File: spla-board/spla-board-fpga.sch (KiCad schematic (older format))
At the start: 35 parts, among them J2 J_JTAG, U1 LFE5U-45F-BG256

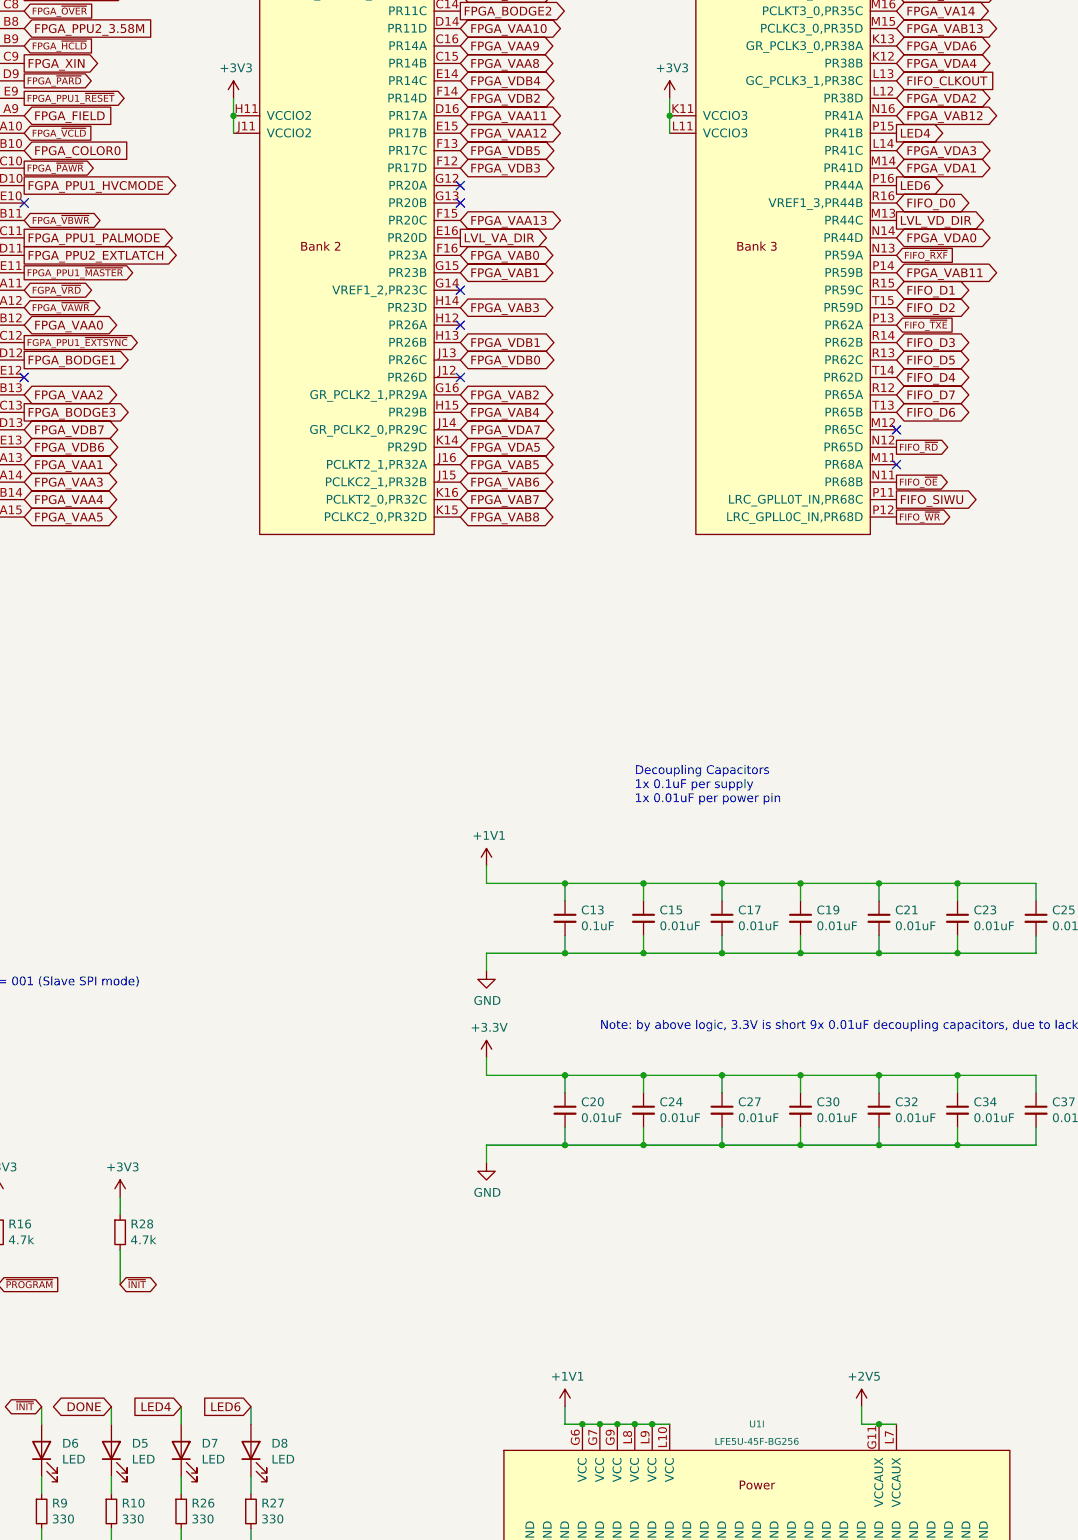
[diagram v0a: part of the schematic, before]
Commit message: schematic: Rename LED[46] to LED[78], to match silkscreen.
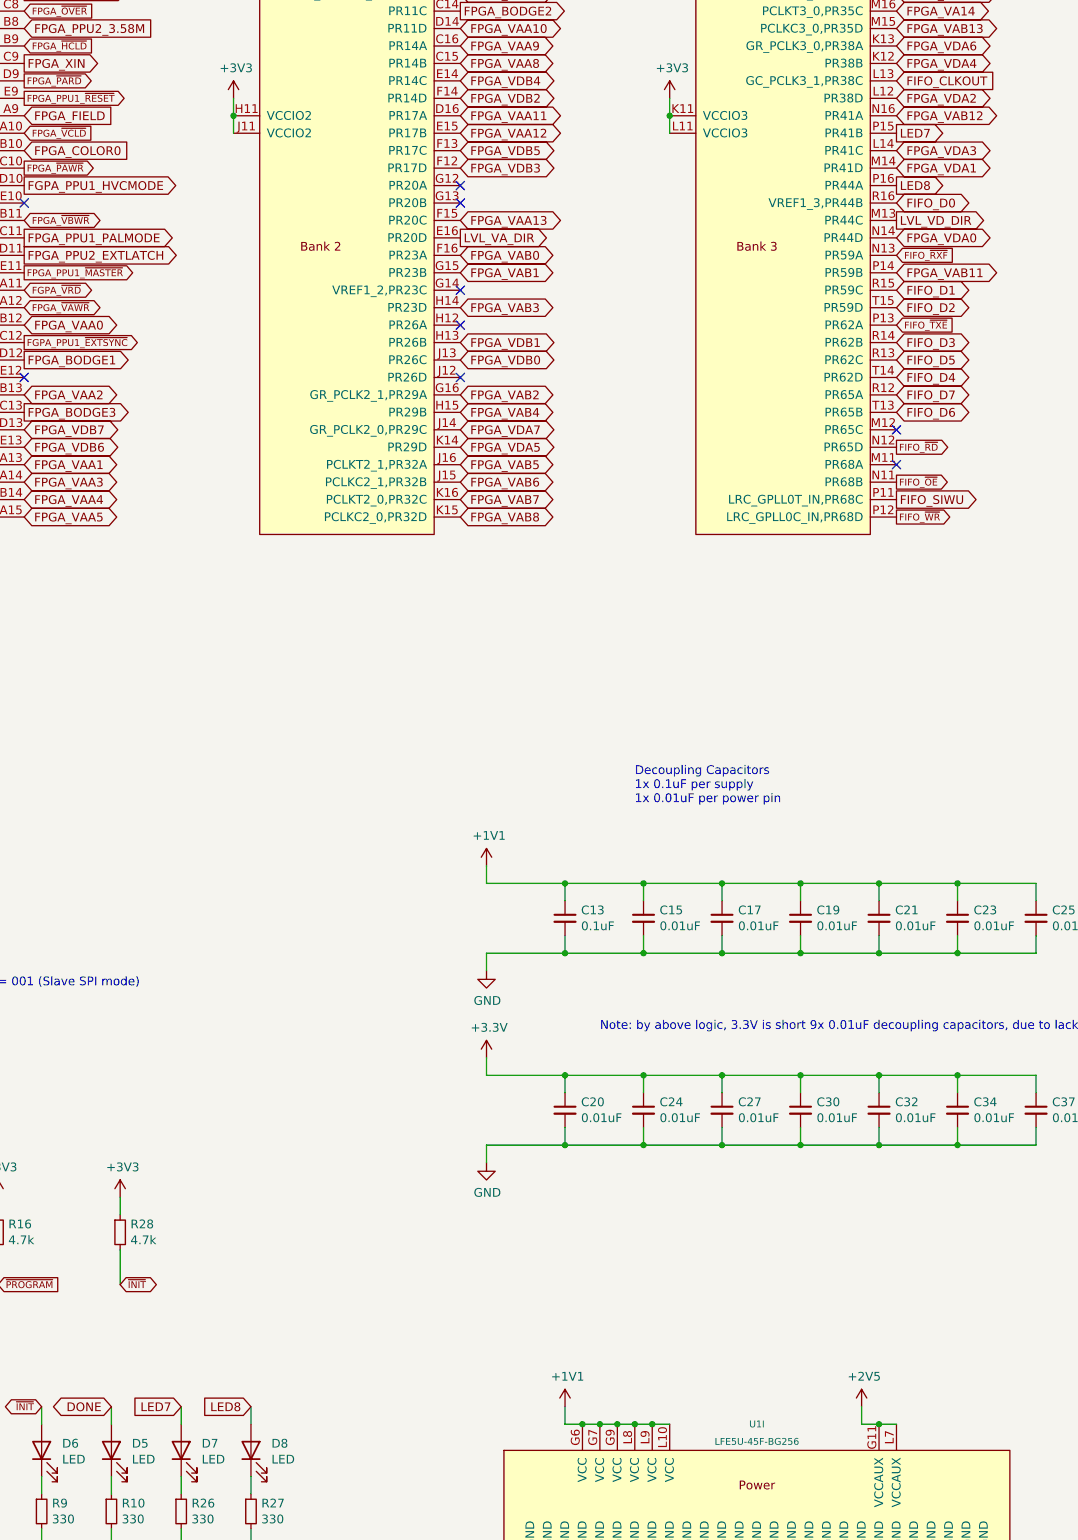
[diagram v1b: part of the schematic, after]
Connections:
- net LED4 renamed LED7
- net LED6 renamed LED8
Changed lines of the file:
@@
 	5950 9500 5950 9600
 Text GLabel 5550 9500 0    50   Input ~ 0
-LED4
+LED7
 Text GLabel 5950 9500 0    50   Input ~ 0
-LED6
+LED8
 Text GLabel 9650 2200 2    50   Output ~ 0
-LED4
+LED7
 Text GLabel 9650 2500 2    50   Output ~ 0
-LED6
+LED8
 NoConn ~ 9650 4100
 NoConn ~ 9650 3900

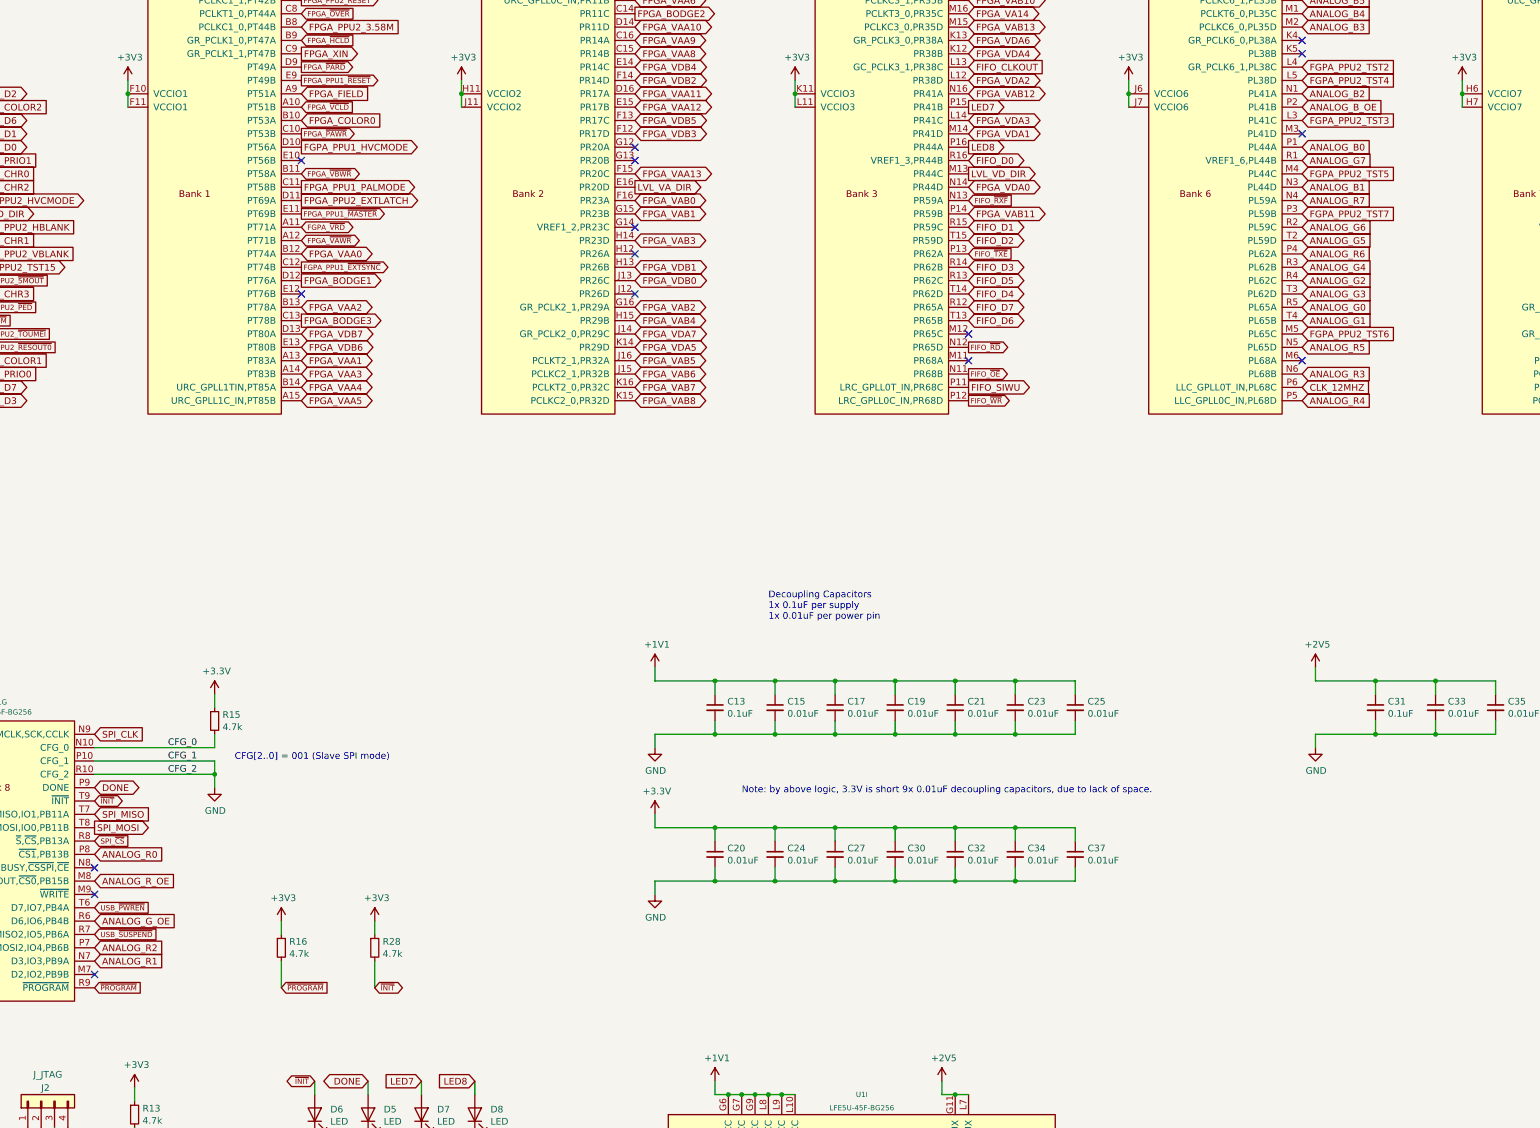
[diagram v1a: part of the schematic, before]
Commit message: schematic/pcb: Consolidate analog output-enable nets, and add a pullup resistor.
Note that this leaves two FPGA pins unused, which I'll need to correct later.
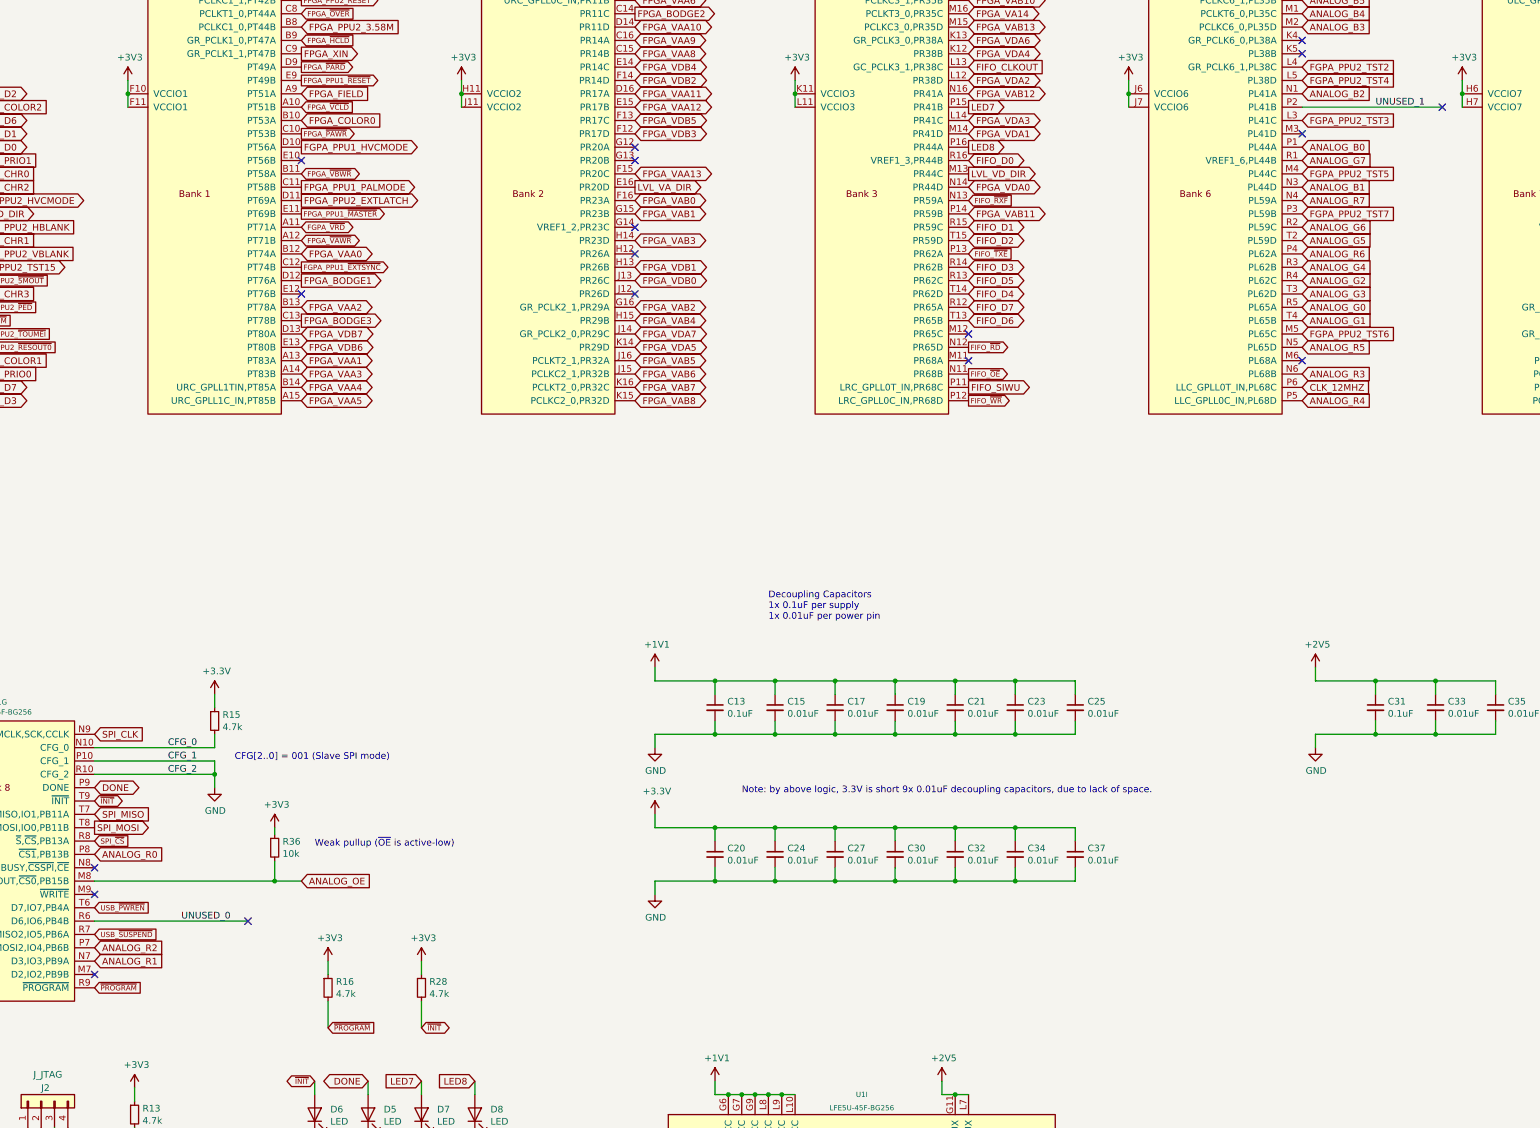
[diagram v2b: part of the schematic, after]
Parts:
- added R36: 10k, Resistor_SMD:R_0603_1608Metric, symbol Device:R_Small
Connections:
- net +3V3: now also R36.1
- net ANALOG_B_OE renamed UNUSED_1
- net ANALOG_G_OE renamed UNUSED_0
- net ANALOG_R_OE renamed ANALOG_OE
- net ANALOG_OE: now also R36.2
- no-connect marks 18 -> 20
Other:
- note added: "Weak pullup (~OE~ is active-low)"
- moved on the sheet: R16, R28
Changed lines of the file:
@@
 Text GLabel 12150 4300 2    50   Input ~ 0
 CLK_12MHZ
-Text GLabel 12150 2200 2    50   Input ~ 0
-ANALOG_B_OE
 Wire Wire Line
 	13350 2100 13350 2200
@@
 Text GLabel 14650 4400 2    50   Input ~ 0
 ANALOG_B7
-Text GLabel 3100 8300 2    50   Input ~ 0
-ANALOG_G_OE
-Text GLabel 3100 8000 2    50   Input ~ 0
-ANALOG_R_OE
+Text GLabel 4650 8000 2    50   Input ~ 0
+ANALOG_OE
 Text GLabel 12150 3700 2    50   Input ~ 0
 ANALOG_G0
@@
 Wire Wire Line
 	4000 6600 4000 6700
-Text GLabel 4500 8800 2    39   Input ~ 0
+Text GLabel 4850 9100 2    39   Input ~ 0
 ~PROGRAM
 Wire Wire Line
-	4500 8800 4500 8600
+	4850 9100 4850 8900
 $Comp
 L Device:R_Small R?
 U 1 1 5EB9F9F9
-P 4500 8500
+P 4850 8800
 AR Path="/5E4F712F/5EB9F9F9" Ref="R?"  Part="1"
 AR Path="/5E50D39B/5EB9F9F9" Ref="R?"  Part="1"
 AR Path="/5E4D8358/5EB9F9F9" Ref="R16"  Part="1"
-F 0 "R16" H 4559 8546 50  0000 L CNN
-F 1 "4.7k" H 4559 8455 50  0000 L CNN
-F 2 "Resistor_SMD:R_0603_1608Metric" H 4500 8500 50  0001 C CNN
-F 3 "~" H 4500 8500 50  0001 C CNN
-F 4 "RMCF0603JT4K70CT-ND" H 4500 8500 50  0001 C CNN "Digikey"
-F 5 "Stackpole Electronics Inc" H 4500 8500 50  0001 C CNN "Manufacturer"
-F 6 "RMCF0603JT4K70" H 4500 8500 50  0001 C CNN "Manufacturer Id"
-	1    4500 8500
+F 0 "R16" H 4909 8846 50  0000 L CNN
+F 1 "4.7k" H 4909 8755 50  0000 L CNN
+F 2 "Resistor_SMD:R_0603_1608Metric" H 4850 8800 50  0001 C CNN
+F 3 "~" H 4850 8800 50  0001 C CNN
+F 4 "RMCF0603JT4K70CT-ND" H 4850 8800 50  0001 C CNN "Digikey"
+F 5 "Stackpole Electronics Inc" H 4850 8800 50  0001 C CNN "Manufacturer"
+F 6 "RMCF0603JT4K70" H 4850 8800 50  0001 C CNN "Manufacturer Id"
+	1    4850 8800
 	1    0    0    -1
 $EndComp
@@
 L power:+3V3 #PWR0214
 U 1 1 5EBA4221
-P 4500 8300
-F 0 "#PWR0214" H 4500 8150 50  0001 C CNN
-F 1 "+3V3" H 4515 8473 50  0000 C CNN
-F 2 "" H 4500 8300 50  0001 C CNN
-F 3 "" H 4500 8300 50  0001 C CNN
-	1    4500 8300
-	1    0    0    -1
-$EndComp
-Wire Wire Line
-	4500 8300 4500 8400
-Text GLabel 5200 8800 2    39   BiDi ~ 0
+P 4850 8600
+F 0 "#PWR0214" H 4850 8450 50  0001 C CNN
+F 1 "+3V3" H 4865 8773 50  0000 C CNN
+F 2 "" H 4850 8600 50  0001 C CNN
+F 3 "" H 4850 8600 50  0001 C CNN
+	1    4850 8600
+	1    0    0    -1
+$EndComp
+Wire Wire Line
+	4850 8600 4850 8700
+Text GLabel 5550 9100 2    39   BiDi ~ 0
 ~INIT
 Wire Wire Line
-	5200 8800 5200 8600
+	5550 9100 5550 8900
 $Comp
 L Device:R_Small R?
 U 1 1 5EBAC32F
-P 5200 8500
+P 5550 8800
 AR Path="/5E4F712F/5EBAC32F" Ref="R?"  Part="1"
 AR Path="/5E50D39B/5EBAC32F" Ref="R?"  Part="1"
 AR Path="/5E4D8358/5EBAC32F" Ref="R28"  Part="1"
-F 0 "R28" H 5259 8546 50  0000 L CNN
-F 1 "4.7k" H 5259 8455 50  0000 L CNN
-F 2 "Resistor_SMD:R_0603_1608Metric" H 5200 8500 50  0001 C CNN
-F 3 "~" H 5200 8500 50  0001 C CNN
-F 4 "RMCF0603JT4K70CT-ND" H 5200 8500 50  0001 C CNN "Digikey"
-F 5 "Stackpole Electronics Inc" H 5200 8500 50  0001 C CNN "Manufacturer"
-F 6 "RMCF0603JT4K70" H 5200 8500 50  0001 C CNN "Manufacturer Id"
-	1    5200 8500
+F 0 "R28" H 5609 8846 50  0000 L CNN
+F 1 "4.7k" H 5609 8755 50  0000 L CNN
+F 2 "Resistor_SMD:R_0603_1608Metric" H 5550 8800 50  0001 C CNN
+F 3 "~" H 5550 8800 50  0001 C CNN
+F 4 "RMCF0603JT4K70CT-ND" H 5550 8800 50  0001 C CNN "Digikey"
+F 5 "Stackpole Electronics Inc" H 5550 8800 50  0001 C CNN "Manufacturer"
+F 6 "RMCF0603JT4K70" H 5550 8800 50  0001 C CNN "Manufacturer Id"
+	1    5550 8800
 	1    0    0    -1
 $EndComp
@@
 L power:+3V3 #PWR0215
 U 1 1 5EBAC339
-P 5200 8300
-F 0 "#PWR0215" H 5200 8150 50  0001 C CNN
-F 1 "+3V3" H 5215 8473 50  0000 C CNN
-F 2 "" H 5200 8300 50  0001 C CNN
-F 3 "" H 5200 8300 50  0001 C CNN
-	1    5200 8300
-	1    0    0    -1
-$EndComp
-Wire Wire Line
-	5200 8300 5200 8400
+P 5550 8600
+F 0 "#PWR0215" H 5550 8450 50  0001 C CNN
+F 1 "+3V3" H 5565 8773 50  0000 C CNN
+F 2 "" H 5550 8600 50  0001 C CNN
+F 3 "" H 5550 8600 50  0001 C CNN
+	1    5550 8600
+	1    0    0    -1
+$EndComp
+Wire Wire Line
+	5550 8600 5550 8700
 Text Label 3650 7000 0    50   ~ 0
 CFG_0
@@
 Wire Wire Line
 	14700 6100 14700 6000
+Wire Wire Line
+	3100 8300 4250 8300
+NoConn ~ 4250 8300
+Text Label 3750 8300 0    50   ~ 0
+UNUSED_0
+Wire Wire Line
+	12150 2200 13200 2200
+NoConn ~ 13200 2200
+Text Label 12700 2200 0    50   ~ 0
+UNUSED_1
+Wire Wire Line
+	4650 8000 4450 8000
+$Comp
+L Device:R_Small R36
+U 1 1 5F3B8BD4
+P 4450 7750
+F 0 "R36" H 4509 7796 50  0000 L CNN
+F 1 "10k" H 4509 7705 50  0000 L CNN
+F 2 "Resistor_SMD:R_0603_1608Metric" H 4450 7750 50  0001 C CNN
+F 3 "~" H 4450 7750 50  0001 C CNN
+F 4 "RMCF0603JT10K0CT-ND" H 4450 7750 50  0001 C CNN "Digikey"
+F 5 "Stackpole Electronics Inc" H 4450 7750 50  0001 C CNN "Manufacturer"
+F 6 "RMCF0603JT10K0" H 4450 7750 50  0001 C CNN "Manufacturer Id"
+	1    4450 7750
+	1    0    0    -1
+$EndComp
+Wire Wire Line
+	4450 7850 4450 8000
+Connection ~ 4450 8000
+Wire Wire Line
+	4450 8000 3100 8000
+Wire Wire Line
+	4450 7650 4450 7600
+$Comp
+L power:+3V3 #PWR0234
+U 1 1 5F3EE61D
+P 4450 7600
+F 0 "#PWR0234" H 4450 7450 50  0001 C CNN
+F 1 "+3V3" H 4465 7773 50  0000 C CNN
+F 2 "" H 4450 7600 50  0001 C CNN
+F 3 "" H 4450 7600 50  0001 C CNN
+	1    4450 7600
+	1    0    0    -1
+$EndComp
+Text Notes 4750 7750 0    50   ~ 0
+Weak pullup (~OE~ is active-low)
 $EndSCHEMATC
